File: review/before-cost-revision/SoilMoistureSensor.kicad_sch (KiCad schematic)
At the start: 51 parts, among them J1 Conn_01x02, J2 Conn_01x04, J3 Conn_01x02, J4 PCB capacitive probe, Q1 AO3401A, SW1 TS-1088-AR02016, SW2 TS-1088-AR02016, U1 BQ25570, U2 ESP32-C3-WROOM-02-N4, U3 TLC555CDR, U4 TPS62842DGRR

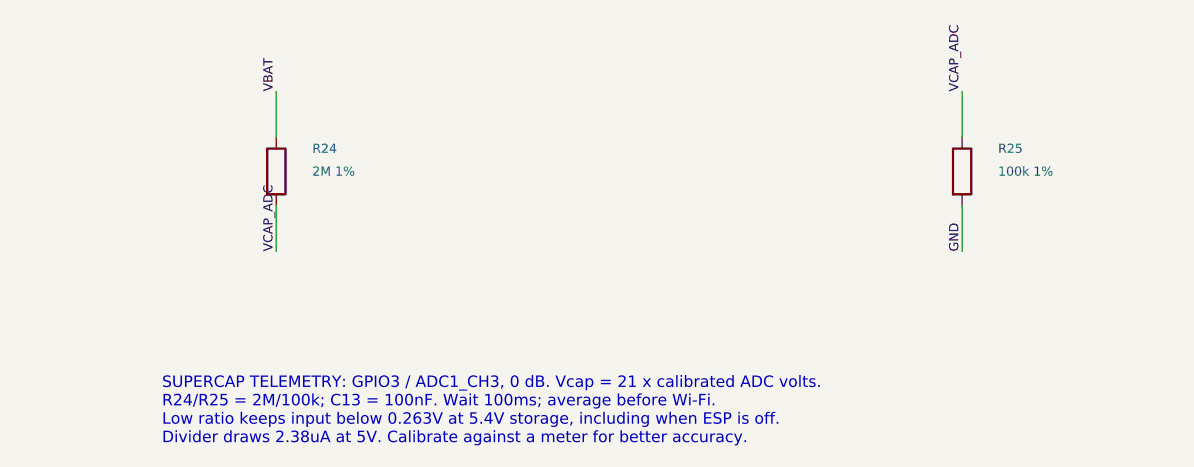
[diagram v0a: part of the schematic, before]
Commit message: reworked some parts to get jlcpcb basic, reworked inductors
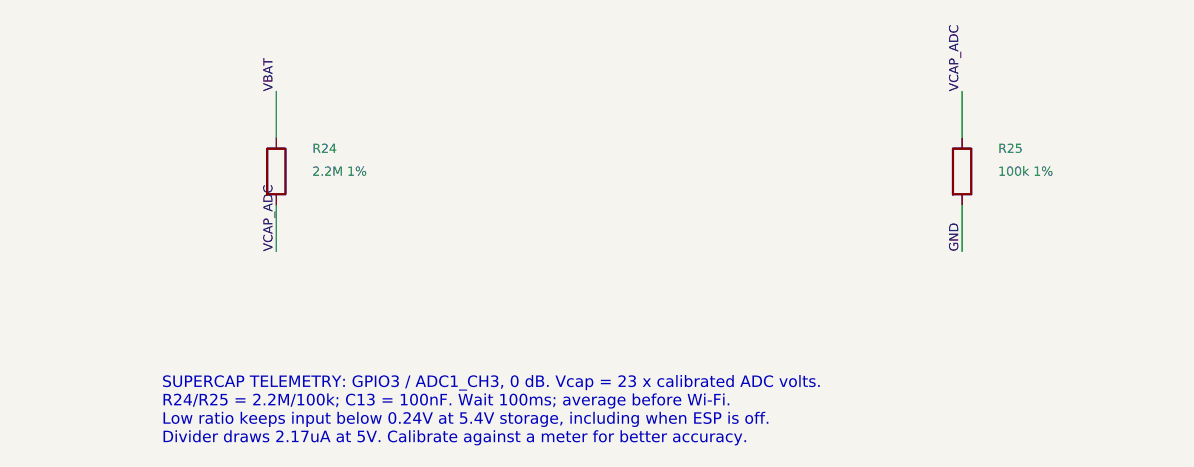
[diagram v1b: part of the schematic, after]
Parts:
- C10, C3, C5, C8, C9: LCSC C49678 -> C1711; MPN CC0805KRX7R9BB104 -> CL21B104KBCNNNC; Manufacturer Yageo -> Samsung Electro-Mechanics; Source https://www.lcsc.com/product-detail/C49678.html -> https://www.lcsc.com/product-detail/C1711.html
- C4: LCSC C97905 -> C1845387; MPN GRM2195C1H103JA01D -> CGA4C2C0G1H103J060AA; Manufacturer Murata Electronics -> TDK; Source https://www.lcsc.com/product-detail/C97905.html -> https://www.lcsc.com/product-detail/C1845387.html
- L1: footprint Inductor_SMD:L_Changjiang_FNR4018S -> Inductor_SMD:L_Coilcraft_LPS4018; LCSC C167883 -> C5278935; MPN FNR4030S220MT -> LPS4018-223MRC; Manufacturer Changjiang Microelectronics -> Coilcraft; Source https://www.lcsc.com/product-detail/C167883.html -> https://www.lcsc.com/product-detail/C5278935.html
- L2: footprint Inductor_SMD:L_Changjiang_FNR4018S -> Inductor_SMD:L_Coilcraft_LPS4018; LCSC C167804 -> C4354938; MPN FNR4018S2R2MT -> LPS4018-222MRC; Manufacturer Changjiang Microelectronics -> Coilcraft; Source https://www.lcsc.com/product-detail/C167804.html -> https://www.lcsc.com/product-detail/C4354938.html
- R24: value 2M 1% -> 2.2M 1%; LCSC C22976 -> C22938; MPN 0603WAF2004T5E -> 0603WAF2204T5E; Source https://www.lcsc.com/product-detail/C22976.html -> https://www.lcsc.com/product-detail/C22938.html
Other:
- note added: "SUPERCAP TELEMETRY: GPIO3 / ADC1_CH3, 0 dB. Vcap = 23 x calibrated ADC volts. R24/R25 = 2.2M/100k; C13 = 100nF. Wait 100ms; average before Wi-Fi. Low ratio keeps input below 0.24V at 5.4V storage, including when ESP is off. Divider draws 2.17uA at 5V. Calibrate against a meter for better accuracy."
- note removed: "SUPERCAP TELEMETRY: GPIO3 / ADC1_CH3, 0 dB. Vcap = 21 x calibrated ADC volts. R24/R25 = 2M/100k; C13 = 100nF. Wait 100ms; average before Wi-Fi. Low ratio keeps input below 0.263V at 5.4V storage, including when ESP is off. Divider draws 2.38uA at 5V. Calibrate against a meter for better accuracy."
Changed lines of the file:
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@@
 			)
 		)
-		(property "Footprint" "Inductor_SMD:L_Changjiang_FNR4018S"
+		(property "Footprint" "Inductor_SMD:L_Coilcraft_LPS4018"
 			(at 42.1 81.28 0)
 			(effects
@@
 			)
 		)
-		(property "Manufacturer" "Changjiang Microelectronics"
+		(property "Manufacturer" "Coilcraft"
 			(at 38.1 81.28 0)
 			(effects
@@
 			)
 		)
-		(property "MPN" "FNR4030S220MT"
+		(property "MPN" "LPS4018-223MRC"
 			(at 38.1 81.28 0)
 			(effects
@@
 			)
 		)
-		(property "LCSC" "C167883"
+		(property "LCSC" "C5278935"
 			(at 38.1 81.28 0)
 			(effects
@@
 			)
 		)
-		(property "Source" "https://www.lcsc.com/product-detail/C167883.html"
+		(property "Source" "https://www.lcsc.com/product-detail/C5278935.html"
 			(at 38.1 81.28 0)
 			(effects
@@
 			)
 		)
-		(property "Manufacturer" "Yageo"
+		(property "Manufacturer" "Samsung Electro-Mechanics"
 			(at 134.62 137.16 0)
 			(effects
@@
 			)
 		)
-		(property "MPN" "CC0805KRX7R9BB104"
+		(property "MPN" "CL21B104KBCNNNC"
 			(at 134.62 137.16 0)
 			(effects
@@
 			)
 		)
-		(property "LCSC" "C49678"
+		(property "LCSC" "C1711"
 			(at 134.62 137.16 0)
 			(effects
@@
 			)
 		)
-		(property "Source" "https://www.lcsc.com/product-detail/C49678.html"
+		(property "Source" "https://www.lcsc.com/product-detail/C1711.html"
 			(at 134.62 137.16 0)
 			(effects
@@
 			)
 		)
-		(property "Manufacturer" "Murata Electronics"
+		(property "Manufacturer" "TDK"
 			(at 180.34 137.16 0)
 			(effects
@@
 			)
 		)
-		(property "MPN" "GRM2195C1H103JA01D"
+		(property "MPN" "CGA4C2C0G1H103J060AA"
 			(at 180.34 137.16 0)
 			(effects
@@
 			)
 		)
-		(property "LCSC" "C97905"
+		(property "LCSC" "C1845387"
 			(at 180.34 137.16 0)
 			(effects
@@
 			)
 		)
-		(property "Source" "https://www.lcsc.com/product-detail/C97905.html"
+		(property "Source" "https://www.lcsc.com/product-detail/C1845387.html"
 			(at 180.34 137.16 0)
 			(effects
@@
 			)
 		)
-		(property "Manufacturer" "Yageo"
+		(property "Manufacturer" "Samsung Electro-Mechanics"
 			(at 226.06 137.16 0)
 			(effects
@@
 			)
 		)
-		(property "MPN" "CC0805KRX7R9BB104"
+		(property "MPN" "CL21B104KBCNNNC"
 			(at 226.06 137.16 0)
 			(effects
@@
 			)
 		)
-		(property "LCSC" "C49678"
+		(property "LCSC" "C1711"
 			(at 226.06 137.16 0)
 			(effects
@@
 			)
 		)
-		(property "Source" "https://www.lcsc.com/product-detail/C49678.html"
+		(property "Source" "https://www.lcsc.com/product-detail/C1711.html"
 			(at 226.06 137.16 0)
 			(effects
@@
 			)
 		)
-		(property "Manufacturer" "Yageo"
+		(property "Manufacturer" "Samsung Electro-Mechanics"
 			(at 330.2 83.82 0)
 			(effects
@@
 			)
 		)
-		(property "MPN" "CC0805KRX7R9BB104"
+		(property "MPN" "CL21B104KBCNNNC"
 			(at 330.2 83.82 0)
 			(effects
@@
 			)
 		)
-		(property "LCSC" "C49678"
+		(property "LCSC" "C1711"
 			(at 330.2 83.82 0)
 			(effects
@@
 			)
 		)
-		(property "Source" "https://www.lcsc.com/product-detail/C49678.html"
+		(property "Source" "https://www.lcsc.com/product-detail/C1711.html"
 			(at 330.2 83.82 0)
 			(effects
@@
 			)
 		)
-		(property "Manufacturer" "Yageo"
+		(property "Manufacturer" "Samsung Electro-Mechanics"
 			(at 330.2 154.94 0)
 			(effects
@@
 			)
 		)
-		(property "MPN" "CC0805KRX7R9BB104"
+		(property "MPN" "CL21B104KBCNNNC"
 			(at 330.2 154.94 0)
 			(effects
@@
 			)
 		)
-		(property "LCSC" "C49678"
+		(property "LCSC" "C1711"
 			(at 330.2 154.94 0)
 			(effects
@@
 			)
 		)
-		(property "Source" "https://www.lcsc.com/product-detail/C49678.html"
+		(property "Source" "https://www.lcsc.com/product-detail/C1711.html"
 			(at 330.2 154.94 0)
 			(effects
@@
 			)
 		)
-		(property "Footprint" "Inductor_SMD:L_Changjiang_FNR4018S"
+		(property "Footprint" "Inductor_SMD:L_Coilcraft_LPS4018"
 			(at 181.8 205.74 0)
 			(effects
@@
 			)
 		)
-		(property "Manufacturer" "Changjiang Microelectronics"
+		(property "Manufacturer" "Coilcraft"
 			(at 177.8 205.74 0)
 			(effects
@@
 			)
 		)
-		(property "MPN" "FNR4018S2R2MT"
+		(property "MPN" "LPS4018-222MRC"
 			(at 177.8 205.74 0)
 			(effects
@@
 			)
 		)
-		(property "LCSC" "C167804"
+		(property "LCSC" "C4354938"
 			(at 177.8 205.74 0)
 			(effects
@@
 			)
 		)
-		(property "Source" "https://www.lcsc.com/product-detail/C167804.html"
+		(property "Source" "https://www.lcsc.com/product-detail/C4354938.html"
 			(at 177.8 205.74 0)
 			(effects
@@
 			)
 		)
-		(property "Manufacturer" "Yageo"
+		(property "Manufacturer" "Samsung Electro-Mechanics"
 			(at 353.06 287.02 0)
 			(effects
@@
 			)
 		)
-		(property "MPN" "CC0805KRX7R9BB104"
+		(property "MPN" "CL21B104KBCNNNC"
 			(at 353.06 287.02 0)
 			(effects
@@
 			)
 		)
-		(property "LCSC" "C49678"
+		(property "LCSC" "C1711"
 			(at 353.06 287.02 0)
 			(effects
@@
 			)
 		)
-		(property "Source" "https://www.lcsc.com/product-detail/C49678.html"
+		(property "Source" "https://www.lcsc.com/product-detail/C1711.html"
 			(at 353.06 287.02 0)
 			(effects
@@
 			)
 		)
-		(property "Value" "2M 1%"
+		(property "Value" "2.2M 1%"
 			(at 334.2 391.16 0)
 			(effects
@@
 			)
 		)
-		(property "MPN" "0603WAF2004T5E"
+		(property "MPN" "0603WAF2204T5E"
 			(at 330.2 391.16 0)
 			(effects
@@
 			)
 		)
-		(property "LCSC" "C22976"
+		(property "LCSC" "C22938"
 			(at 330.2 391.16 0)
 			(effects
@@
 			)
 		)
-		(property "Source" "https://www.lcsc.com/product-detail/C22976.html"
+		(property "Source" "https://www.lcsc.com/product-detail/C22938.html"
 			(at 330.2 391.16 0)
 			(effects
@@
 		)
 	)
-	(text "SUPERCAP TELEMETRY: GPIO3 / ADC1_CH3, 0 dB. Vcap = 21 x calibrated ADC volts.\nR24/R25 = 2M/100k; C13 = 100nF. Wait 100ms; average before Wi-Fi.\nLow ratio keeps input below 0.263V at 5.4V storage, including when ESP is off.\nDivider draws 2.38uA at 5V. Calibrate against a meter for better accuracy."
+	(text "SUPERCAP TELEMETRY: GPIO3 / ADC1_CH3, 0 dB. Vcap = 23 x calibrated ADC volts.\nR24/R25 = 2.2M/100k; C13 = 100nF. Wait 100ms; average before Wi-Fi.\nLow ratio keeps input below 0.24V at 5.4V storage, including when ESP is off.\nDivider draws 2.17uA at 5V. Calibrate against a meter for better accuracy."
 		(at 317.5 414.02 0)
 		(effects
